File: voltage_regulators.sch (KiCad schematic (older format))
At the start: 18 parts, among them J1 Conn_01x02, J2 Conn_01x02, Q1 FDS4141, SW1 SW_SPDT, U1 ST1S10PHR, U2 LM1117-3.3

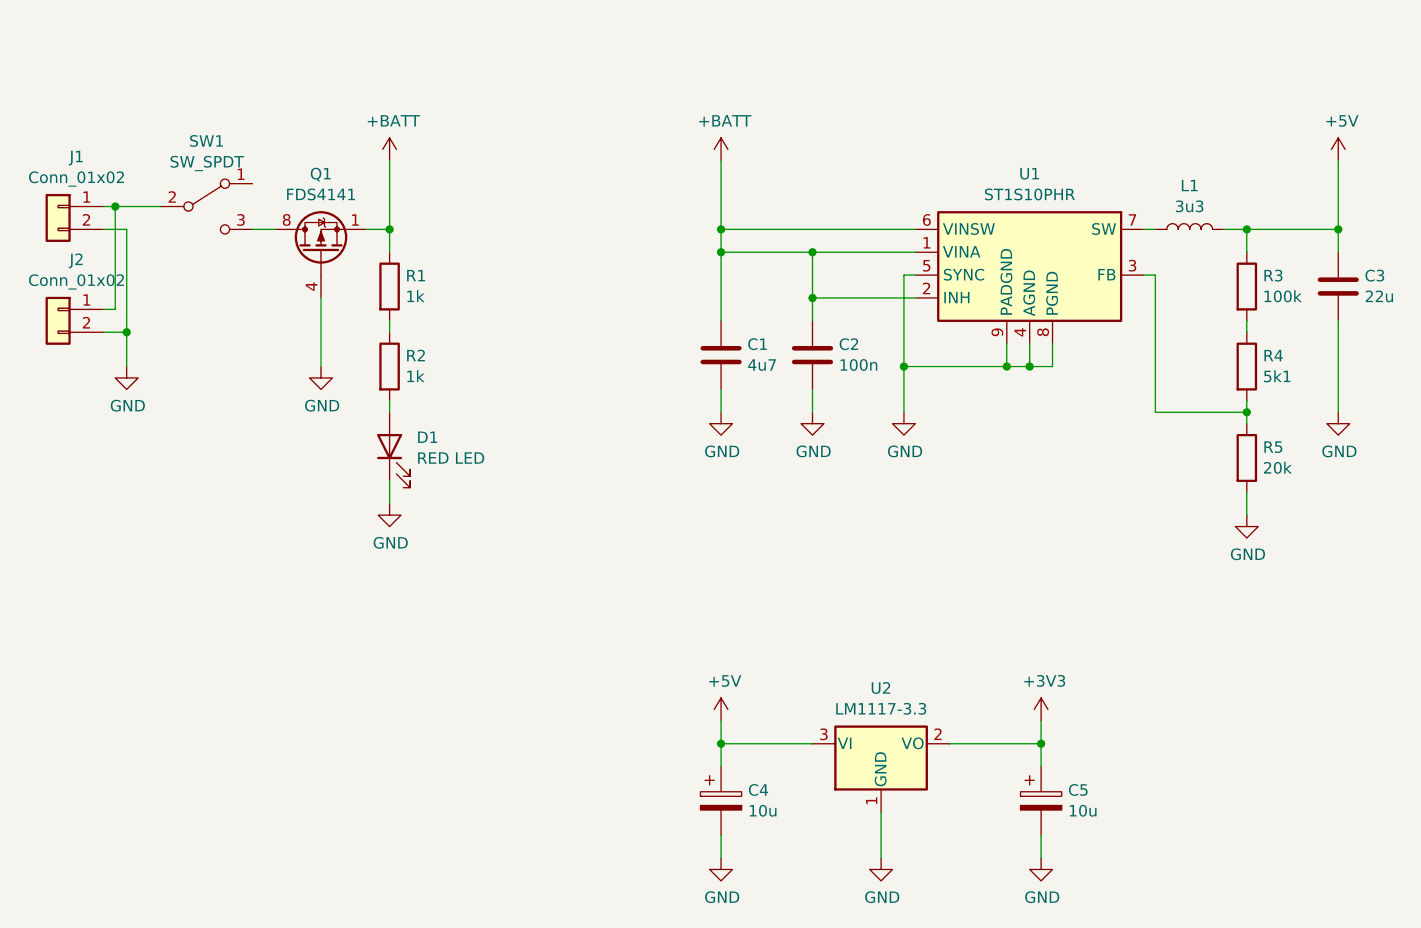
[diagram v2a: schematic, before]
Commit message: Add PCB layout
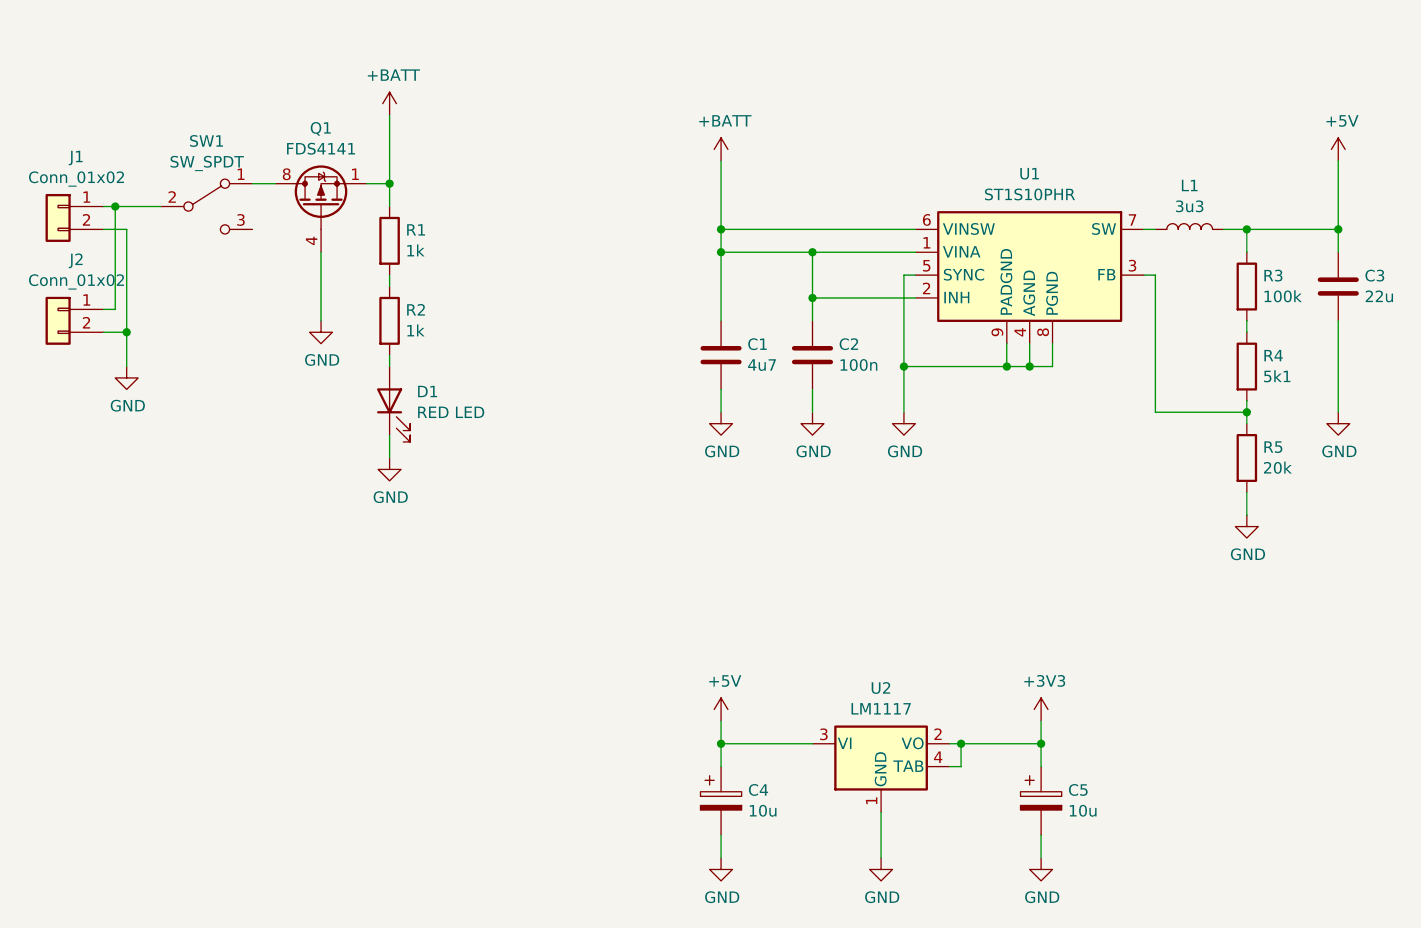
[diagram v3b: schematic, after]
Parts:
- removed U2: LM1117-3.3, Library:SOT-223-4, symbol Regulator_Linear:LM1117-3.3
- added U2: LM1117, Library:SOT-223-4, symbol Symbol_Library:LM1117
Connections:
- net +3V3: now also U2.2 (VO), U2.4 (TAB)
- net +5V: now also U2.3 (VI)
- net GND: now also U2.1 (GND)
- net at SW1.1 (A): now also Q1.5 (D), Q1.6 (D), Q1.7 (D), Q1.8 (D)
- now unconnected: SW1.3 (C)
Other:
- moved on the sheet: D1, Q1, R1, R2
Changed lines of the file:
@@
 L Transistor_FET:FDS9435A Q1
 U 1 1 60B277D5
-P 3300 2150
-F 0 "Q1" V 3642 2150 50  0000 C CNN
-F 1 "FDS4141" V 3551 2150 50  0000 C CNN
-F 2 "Library:SO-8" H 3500 2075 50  0001 L CIN
-F 3 "https://www.onsemi.com/pub/Collateral/FDS9435A-D.PDF" V 3300 2150 50  0001 L CNN
-	1    3300 2150
+P 3300 1950
+F 0 "Q1" V 3642 1950 50  0000 C CNN
+F 1 "FDS4141" V 3551 1950 50  0000 C CNN
+F 2 "Library:SO-8" H 3500 1875 50  0001 L CIN
+F 3 "https://www.onsemi.com/pub/Collateral/FDS9435A-D.PDF" V 3300 1950 50  0001 L CNN
+	1    3300 1950
 	0    -1   -1   0
 $EndComp
@@
 L Device:R R1
 U 1 1 60B29A16
-P 3600 2300
-F 0 "R1" H 3670 2346 50  0000 L CNN
-F 1 "1k" H 3670 2255 50  0000 L CNN
-F 2 "Library:R_1206" V 3530 2300 50  0001 C CNN
-F 3 "~" H 3600 2300 50  0001 C CNN
-	1    3600 2300
+P 3600 2100
+F 0 "R1" H 3670 2146 50  0000 L CNN
+F 1 "1k" H 3670 2055 50  0000 L CNN
+F 2 "Library:R_1206" V 3530 2100 50  0001 C CNN
+F 3 "~" H 3600 2100 50  0001 C CNN
+	1    3600 2100
 	1    0    0    -1
 $EndComp
@@
 L Device:R R2
 U 1 1 60B2D1FC
-P 3600 2650
-F 0 "R2" H 3670 2696 50  0000 L CNN
-F 1 "1k" H 3670 2605 50  0000 L CNN
-F 2 "Library:R_1206" V 3530 2650 50  0001 C CNN
-F 3 "~" H 3600 2650 50  0001 C CNN
-	1    3600 2650
+P 3600 2450
+F 0 "R2" H 3670 2496 50  0000 L CNN
+F 1 "1k" H 3670 2405 50  0000 L CNN
+F 2 "Library:R_1206" V 3530 2450 50  0001 C CNN
+F 3 "~" H 3600 2450 50  0001 C CNN
+	1    3600 2450
 	1    0    0    -1
 $EndComp
@@
 L Device:LED D1
 U 1 1 60B302CE
-P 3600 3000
-F 0 "D1" V 3639 2882 50  0000 R CNN
-F 1 "RED LED" V 3548 2882 50  0000 R CNN
-F 2 "Library:LED_0805" H 3600 3000 50  0001 C CNN
-F 3 "~" H 3600 3000 50  0001 C CNN
-	1    3600 3000
+P 3600 2800
+F 0 "D1" V 3639 2682 50  0000 R CNN
+F 1 "RED LED" V 3548 2682 50  0000 R CNN
+F 2 "Library:LED_0805" H 3600 2800 50  0001 C CNN
+F 3 "~" H 3600 2800 50  0001 C CNN
+	1    3600 2800
 	0    -1   -1   0
 $EndComp
@@
 L power:+BATT #PWR03
 U 1 1 60B318F0
-P 3600 1750
-F 0 "#PWR03" H 3600 1600 50  0001 C CNN
-F 1 "+BATT" H 3615 1923 50  0000 C CNN
-F 2 "" H 3600 1750 50  0001 C CNN
-F 3 "" H 3600 1750 50  0001 C CNN
-	1    3600 1750
+P 3600 1550
+F 0 "#PWR03" H 3600 1400 50  0001 C CNN
+F 1 "+BATT" H 3615 1723 50  0000 C CNN
+F 2 "" H 3600 1550 50  0001 C CNN
+F 3 "" H 3600 1550 50  0001 C CNN
+	1    3600 1550
 	1    0    0    -1
 $EndComp
@@
 $EndComp
 $Comp
-L Regulator_Linear:LM1117-3.3 U2
-U 1 1 60B404E7
-P 5750 4300
-F 0 "U2" H 5750 4542 50  0000 C CNN
-F 1 "LM1117-3.3" H 5750 4451 50  0000 C CNN
-F 2 "Library:SOT-223-4" H 5750 4300 50  0001 C CNN
-F 3 "http://www.ti.com/lit/ds/symlink/lm1117.pdf" H 5750 4300 50  0001 C CNN
-	1    5750 4300
-	1    0    0    -1
-$EndComp
-$Comp
 L Device:CP C5
 U 1 1 60B41B3F
@@
 L power:GND #PWR02
 U 1 1 60B46A1B
-P 3300 2650
-F 0 "#PWR02" H 3300 2400 50  0001 C CNN
-F 1 "GND" H 3305 2477 50  0000 C CNN
-F 2 "" H 3300 2650 50  0001 C CNN
-F 3 "" H 3300 2650 50  0001 C CNN
-	1    3300 2650
+P 3300 2450
+F 0 "#PWR02" H 3300 2200 50  0001 C CNN
+F 1 "GND" H 3305 2277 50  0000 C CNN
+F 2 "" H 3300 2450 50  0001 C CNN
+F 3 "" H 3300 2450 50  0001 C CNN
+	1    3300 2450
 	1    0    0    -1
 $EndComp
@@
 L power:GND #PWR04
 U 1 1 60B470DF
-P 3600 3250
-F 0 "#PWR04" H 3600 3000 50  0001 C CNN
-F 1 "GND" H 3605 3077 50  0000 C CNN
-F 2 "" H 3600 3250 50  0001 C CNN
-F 3 "" H 3600 3250 50  0001 C CNN
-	1    3600 3250
+P 3600 3050
+F 0 "#PWR04" H 3600 2800 50  0001 C CNN
+F 1 "GND" H 3605 2877 50  0000 C CNN
+F 2 "" H 3600 3050 50  0001 C CNN
+F 3 "" H 3600 3050 50  0001 C CNN
+	1    3600 3050
 	1    0    0    -1
 $EndComp
@@
 	2450 2050 2350 2050
 Wire Wire Line
-	3000 2050 3100 2050
-Wire Wire Line
-	3500 2050 3600 2050
-Wire Wire Line
-	3600 2050 3600 2150
-Wire Wire Line
-	3600 2450 3600 2500
-Wire Wire Line
-	3600 2800 3600 2850
-Wire Wire Line
-	3600 3150 3600 3250
-Connection ~ 3600 2050
-Wire Wire Line
-	3600 1750 3600 2050
+	3500 1850 3600 1850
+Wire Wire Line
+	3600 1850 3600 1950
+Wire Wire Line
+	3600 2250 3600 2300
+Wire Wire Line
+	3600 2600 3600 2650
+Wire Wire Line
+	3600 2950 3600 3050
+Connection ~ 3600 1850
+Wire Wire Line
+	3600 1550 3600 1850
 Wire Wire Line
 	2450 2500 2450 2650
 Connection ~ 2450 2500
 Wire Wire Line
-	3300 2350 3300 2650
+	3300 2150 3300 2450
 Wire Wire Line
 	6500 2550 6500 2650
@@
 	5050 4300 5050 4400
 Wire Wire Line
-	5750 4600 5750 4800
-Wire Wire Line
-	6050 4300 6450 4300
+	6050 4300 6100 4300
 Wire Wire Line
 	6450 4300 6450 4200
@@
 Wire Wire Line
 	6450 4700 6450 4800
+Wire Wire Line
+	3000 1850 3100 1850
+$Comp
+L Symbol_Library:LM1117 U2
+U 1 1 610CBD46
+P 5750 4300
+F 0 "U2" H 5750 4542 50  0000 C CNN
+F 1 "LM1117" H 5750 4451 50  0000 C CNN
+F 2 "Library:SOT-223-4" H 5750 4300 50  0001 C CNN
+F 3 "http://www.ti.com/lit/ds/symlink/lm1117.pdf" H 5750 4300 50  0001 C CNN
+	1    5750 4300
+	1    0    0    -1
+$EndComp
+Wire Wire Line
+	6050 4400 6100 4400
+Wire Wire Line
+	6100 4400 6100 4300
+Wire Wire Line
+	5750 4600 5750 4800
+Connection ~ 6100 4300
+Wire Wire Line
+	6100 4300 6450 4300
 $EndSCHEMATC

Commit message: Update and rename files
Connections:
- net +BATT: now also J1.1 (Pin_1), SW1.2 (B); no longer C1.1, C2.1, Q1.1 (S), Q1.2 (S), Q1.3 (S), R1.1, U1.1 (VINA), U1.2 (INH), U1.6 (VINSW)
- new net +VSW: C1.1, C2.1, J2.1 (Pin_1), Q1.1 (S), Q1.2 (S), Q1.3 (S), R1.1, U1.1 (VINA), U1.2 (INH), U1.6 (VINSW)
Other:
- moved on the sheet: J2
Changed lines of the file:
@@
 L Connector_Generic:Conn_01x02 J2
 U 1 1 60B238B2
-P 2150 2400
-F 0 "J2" H 2068 2617 50  0000 C CNN
-F 1 "Conn_01x02" H 2068 2526 50  0000 C CNN
-F 2 "Library:Degson_15EDGRC-3.5" H 2150 2400 50  0001 C CNN
-F 3 "~" H 2150 2400 50  0001 C CNN
-	1    2150 2400
+P 2150 1400
+F 0 "J2" H 2068 1617 50  0000 C CNN
+F 1 "Conn_01x02" H 2068 1526 50  0000 C CNN
+F 2 "Library:Degson_15EDGRC-3.5" H 2150 1400 50  0001 C CNN
+F 3 "~" H 2150 1400 50  0001 C CNN
+	1    2150 1400
 	-1   0    0    -1
 $EndComp
@@
 L power:+BATT #PWR03
 U 1 1 60B318F0
-P 3600 1550
-F 0 "#PWR03" H 3600 1400 50  0001 C CNN
-F 1 "+BATT" H 3615 1723 50  0000 C CNN
-F 2 "" H 3600 1550 50  0001 C CNN
-F 3 "" H 3600 1550 50  0001 C CNN
-	1    3600 1550
-	1    0    0    -1
-$EndComp
-$Comp
-L power:+BATT #PWR05
-U 1 1 60B33BB0
-P 5050 1750
-F 0 "#PWR05" H 5050 1600 50  0001 C CNN
-F 1 "+BATT" H 5065 1923 50  0000 C CNN
-F 2 "" H 5050 1750 50  0001 C CNN
-F 3 "" H 5050 1750 50  0001 C CNN
-	1    5050 1750
+P 2550 1900
+F 0 "#PWR03" H 2550 1750 50  0001 C CNN
+F 1 "+BATT" H 2565 2073 50  0000 C CNN
+F 2 "" H 2550 1900 50  0001 C CNN
+F 3 "" H 2550 1900 50  0001 C CNN
+	1    2550 1900
 	1    0    0    -1
 $EndComp
@@
 $EndComp
 Wire Wire Line
-	2350 1950 2400 1950
-Wire Wire Line
-	2350 2400 2400 2400
-Wire Wire Line
-	2400 2400 2400 1950
-Connection ~ 2400 1950
-Wire Wire Line
-	2400 1950 2600 1950
-Wire Wire Line
-	2350 2500 2450 2500
-Wire Wire Line
-	2450 2500 2450 2050
-Wire Wire Line
 	2450 2050 2350 2050
 Wire Wire Line
@@
 	3600 2950 3600 3050
 Connection ~ 3600 1850
-Wire Wire Line
-	3600 1550 3600 1850
-Wire Wire Line
-	2450 2500 2450 2650
-Connection ~ 2450 2500
 Wire Wire Line
 	3300 2150 3300 2450
@@
 Wire Wire Line
 	6100 4300 6450 4300
+Wire Wire Line
+	2350 1950 2550 1950
+Wire Wire Line
+	2450 2050 2450 2650
+Wire Wire Line
+	2450 2050 2450 1500
+Wire Wire Line
+	2450 1500 2350 1500
+Connection ~ 2450 2050
+Wire Wire Line
+	2350 1400 3600 1400
+Wire Wire Line
+	3600 1400 3600 1850
+Wire Wire Line
+	3600 1400 3600 1350
+Connection ~ 3600 1400
+$Comp
+L power:+VSW #PWR?
+U 1 1 60F17918
+P 3600 1350
+F 0 "#PWR?" H 3600 1200 50  0001 C CNN
+F 1 "+VSW" H 3615 1523 50  0000 C CNN
+F 2 "" H 3600 1350 50  0001 C CNN
+F 3 "" H 3600 1350 50  0001 C CNN
+	1    3600 1350
+	1    0    0    -1
+$EndComp
+$Comp
+L power:+VSW #PWR?
+U 1 1 60F1966B
+P 5050 1750
+F 0 "#PWR?" H 5050 1600 50  0001 C CNN
+F 1 "+VSW" H 5065 1923 50  0000 C CNN
+F 2 "" H 5050 1750 50  0001 C CNN
+F 3 "" H 5050 1750 50  0001 C CNN
+	1    5050 1750
+	1    0    0    -1
+$EndComp
+Wire Wire Line
+	2550 1900 2550 1950
+Connection ~ 2550 1950
+Wire Wire Line
+	2550 1950 2600 1950
 $EndSCHEMATC
